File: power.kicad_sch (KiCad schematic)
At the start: 30 parts, among them J2 KYCO-P4S-S, J3 MicroFit_2x02, J3B1 DNI, J4 DC 24V/5A OUT, Q2 IRF9540SPBF, SW1 DNI, U1 MAX5035BUSA, U6 MC78M12BDTG

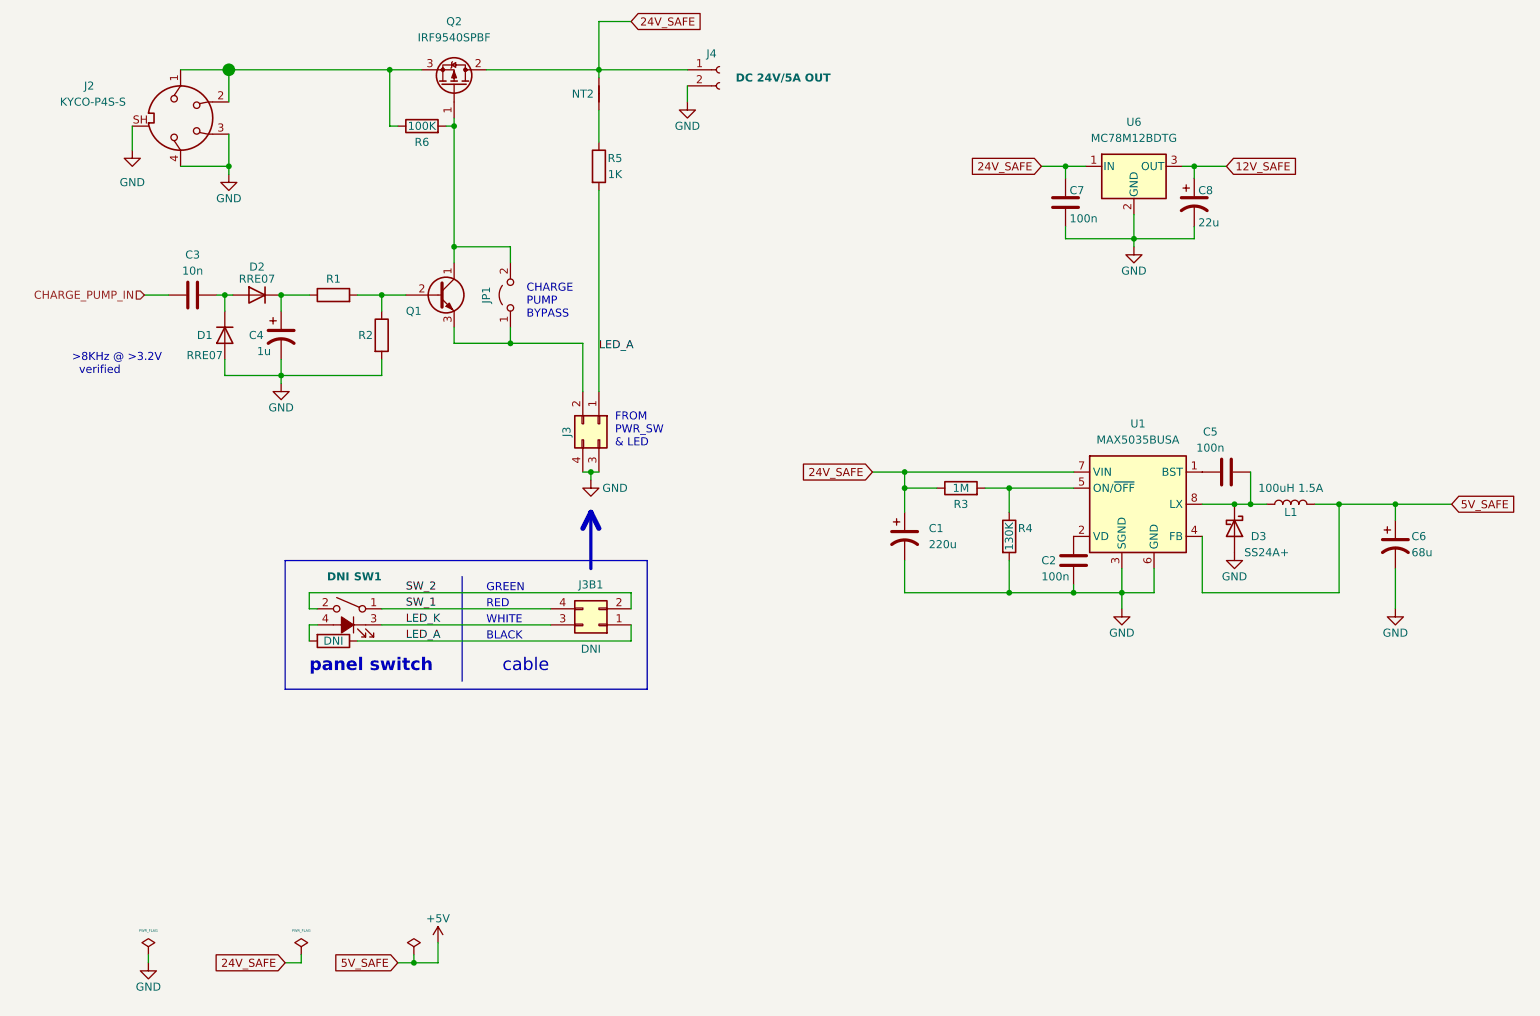
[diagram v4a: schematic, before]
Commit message: Resistor networks changed to 0603 'cause JLCPCB has those as 'basic parts' & aunch of tweaks. (WIP)
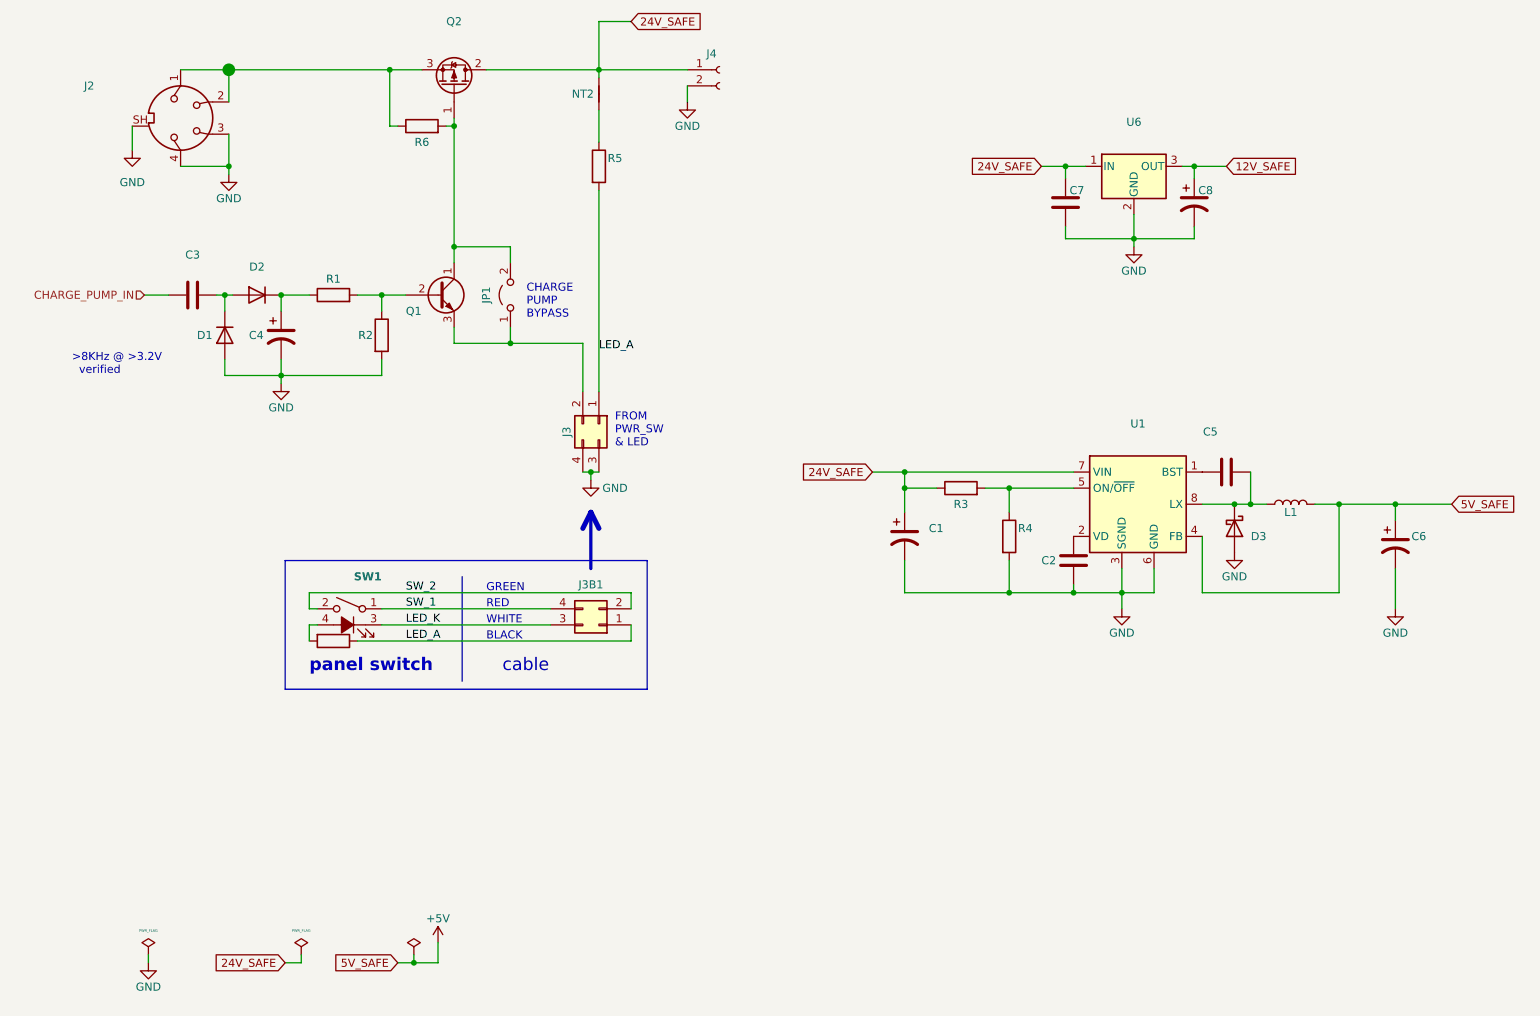
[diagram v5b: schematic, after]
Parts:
- C1: value 220u -> (none); footprint Capacitor_SMD:CP_Elec_8x10.5 -> (none)
- C2, C5, C7: value 100n -> (none); footprint Capacitor_SMD:C_0603_1608Metric -> (none)
- C3: value 10n -> (none); footprint Capacitor_SMD:C_0603_1608Metric -> (none)
- C4: value 1u -> (none); footprint Capacitor_SMD:C_0603_1608Metric -> (none)
- C6: value 68u -> (none); footprint Capacitor_SMD:CP_Elec_6.3x7.7 -> (none)
- C8: value 22u -> (none); footprint Capacitor_SMD:C_0603_1608Metric -> (none)
- D1, D2: value RRE07 -> (none); footprint Diode_SMD:D_SOD-323_HandSoldering -> (none)
- D3: value SS24A+ -> (none); footprint Diode_SMD:D_SMA -> (none)
- J2: value KYCO-P4S-S -> (none); footprint _footprints:KYCON_KPJX-4S-S -> (none)
- J3: value MicroFit_2x02 -> (none); footprint Connector_Molex:Molex_Micro-Fit_3.0_43045-0412_2x02_P3.00mm_Vertical -> (none)
- J3B1, R101, SW1: value DNI -> (none)
- J4: value DC 24V/5A OUT -> (none); footprint TerminalBlock_RND:TerminalBlock_RND_205-00232_1x02_P5.08mm_Horizontal -> (none)
- JP1: value Jumper_2_Bridged -> (none); footprint Connector_PinHeader_2.54mm:PinHeader_2x01_P2.54mm_Vertical -> (none)
- L1: value 100uH 1.5A -> (none); footprint Inductor_SMD:L_12x12mm_H6mm -> (none)
- NT2: value DNI -> (none); footprint _footprints:NetTie-2_SMD_Pad0.3mm -> (none)
- Q1: footprint Package_TO_SOT_THT:TO-92_Inline -> (none)
- Q2: value IRF9540SPBF -> (none); footprint Package_TO_SOT_SMD:TO-263-2 -> (none)
- R1, R2: footprint Resistor_SMD:R_0603_1608Metric -> (none)
- R3: value 1M -> (none); footprint Resistor_SMD:R_0603_1608Metric -> (none)
- R4: value 130K -> (none); footprint Resistor_SMD:R_0603_1608Metric -> (none)
- R5: value 1K -> (none); footprint Resistor_SMD:R_0603_1608Metric -> (none)
- R6: value 100K -> (none); footprint Resistor_SMD:R_0603_1608Metric -> (none)
- U1: value MAX5035BUSA -> (none); footprint Package_SO:SOIC-8_3.9x4.9mm_P1.27mm -> (none)
- U6: value MC78M12BDTG -> (none); footprint Package_TO_SOT_SMD:TO-252-2 -> (none)

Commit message: temp
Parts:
- C1: value (none) -> 220u; Element14 2611399 -> (none)
- C2, C5: value (none) -> 100n; E14PART (none) -> 432210; Element14 432210 -> (none)
- C3: value (none) -> 10n; Element14 1709948 -> (none)
- C4: value (none) -> 1u; Element14 9402080 -> (none)
- C6: value (none) -> 68u; Element14 2507732 -> (none)
- C7: value (none) -> 100n
- C8: value (none) -> 22u
- D1, D2: value (none) -> RRE07; Element14 3407110 -> (none)
- D3: value (none) -> SS24A+; Element14 2748189 -> (none)
- J2: value (none) -> KYCO-P4S-S; E14PART (none) -> 2839851; Element14 2839851 -> (none)
- J3: value (none) -> MicroFit_2x02; E14PART (none) -> 1012247; Element14 1012247 -> (none)
- J3B1, NT2, R101, SW1: value (none) -> DNI
- J4: value (none) -> DC 24V/5A OUT; E14PART (none) -> 2527547; Element14 2527547 -> (none)
- JP1: value (none) -> Jumper_2_Bridged; E14PART (none) -> 9480102; Element14 9480102 -> (none)
- L1: value (none) -> 100uH 1.5A; E14PART (none) -> 1635912; Element14 1635912 -> (none)
- Q1: value (none) -> BC847
- Q2: value (none) -> IRF9540SPBF; E14PART (none) -> 2646350; Element14 2646350 -> (none)
- R1: value (none) -> 6K8; E14PART (none) -> 2073350; Element14 2073350 -> (none)
- R2: value (none) -> 130K; E14PART (none) -> 2073350; Element14 2073350 -> (none)
- R3: value (none) -> 1M; E14PART (none) -> 2447285; Element14 2447285 -> (none)
- R4: value (none) -> 130K; E14PART (none) -> 2073383; Element14 2073383 -> (none)
- R5: value (none) -> 1K; E14PART (none) -> 2447272; Element14 2447272 -> (none)
- R6: value (none) -> 100K; E14PART (none) -> 2073350; Element14 2073350 -> (none)
- U1: value (none) -> MAX5035BUSA; E14PART (none) -> 2799102; Element14 2799102 -> (none)
- U6: value (none) -> MC78M12BDTG; E14PART (none) -> 1652354; Element14 1652354 -> (none)
